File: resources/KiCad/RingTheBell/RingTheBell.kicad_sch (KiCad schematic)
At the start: 12 parts

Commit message: first cut at schematic
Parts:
- added SW1, SW2, SW3, SW4: SW_SPST, symbol Switch:SW_SPST
- renumbered U1 to A4
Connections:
- net at A3.~ (IO1_09), A4. (3V3), R2.2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: now also SW1.1 (A), SW2.1 (A)
- net at A2.~ (IO1_09): now also R6.2
- net at A1.~ (D13): now also R6.1; no longer A2.~ (IO1_09)
- net at A4. (3V3): now also A3.~ (IO1_09)
- net at A3.~ (IO1_09): no longer A4. (3V3)
- new net: A1.~ (D13), A2.~ (IO1_09), SW3.1 (A), SW4.1 (A)
- new net: A1.~ (D13), SW4.2 (B)
- new net: A1.~ (D13), A2.~ (IO1_09) (x3)
- new net: A1.~ (D13), SW3.2 (B)
- new net: A4. (3V3), SW2.2 (B)
- new net: A4. (3V3), SW1.2 (B)
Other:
- note added: "Purple-Mallet"
- note added: "White-Bell"
- note added: "Yellow"
- moved on the sheet: A3A, A4, LS1, R1, R2, R3, R4, R5

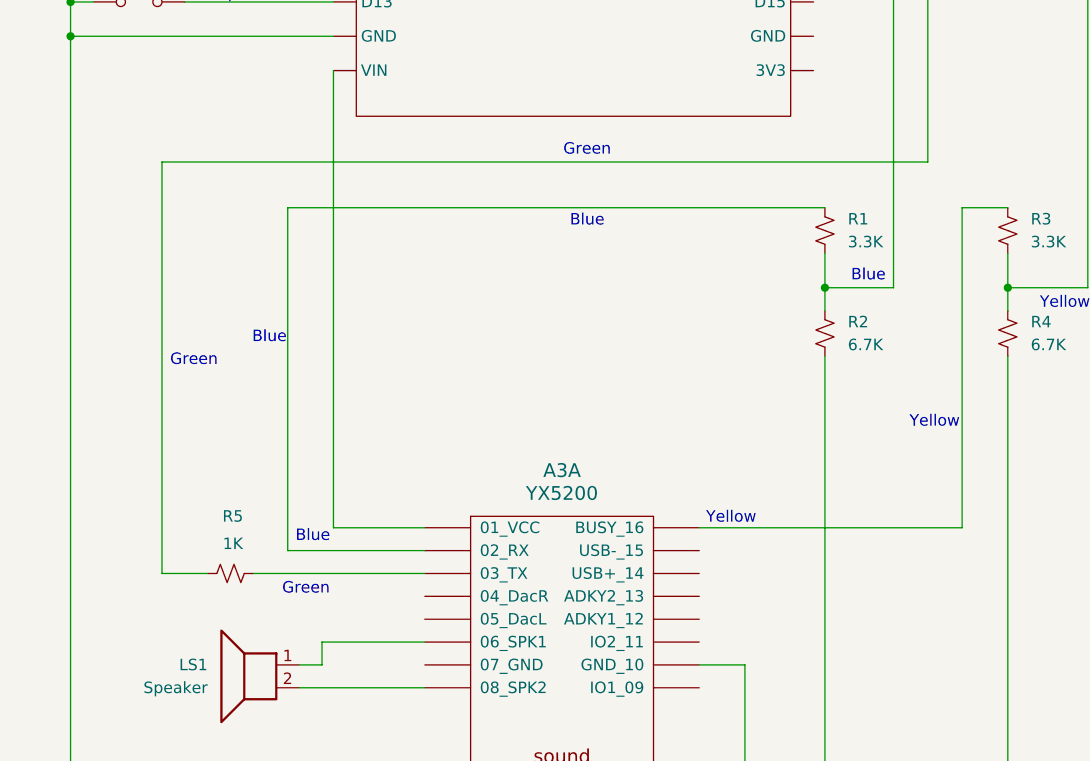
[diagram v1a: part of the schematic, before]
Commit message: fix error in ESP32 TX/RX
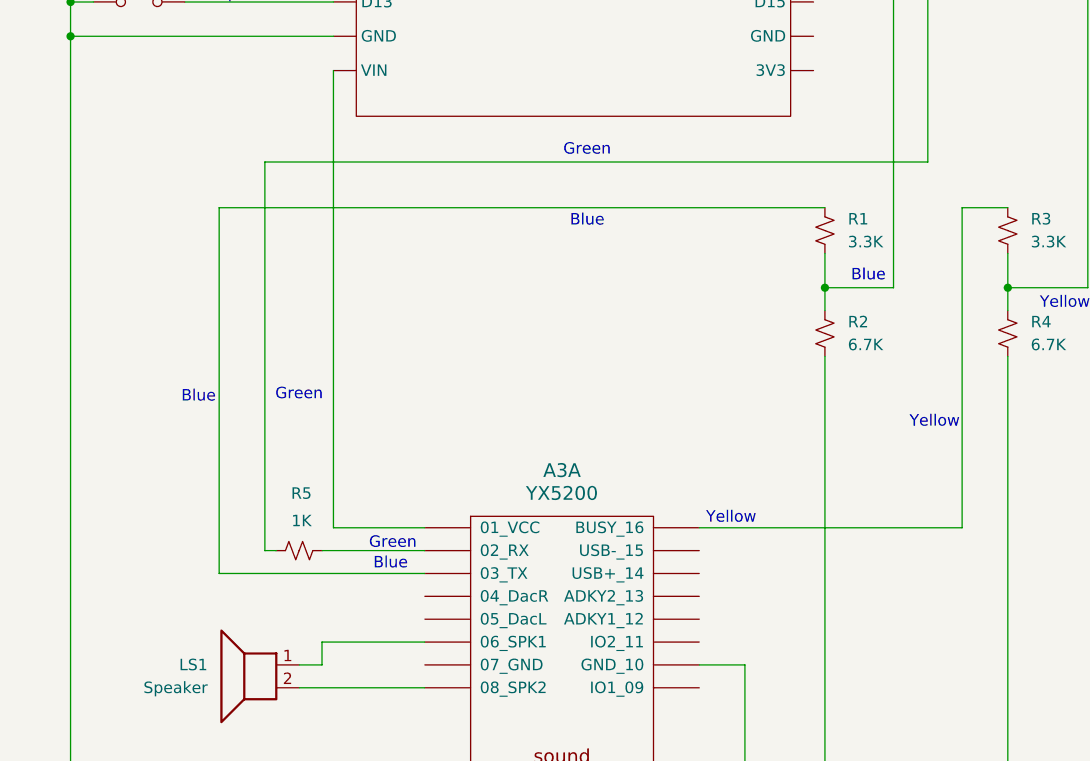
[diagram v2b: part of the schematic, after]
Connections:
- net at A2.~ (IO1_09): now also R6.2
- net at A1.~ (D13): now also R6.1; no longer A2.~ (IO1_09)
- net at A4. (3V3): now also A3.~ (IO1_09)
- net at A3.~ (IO1_09): no longer A4. (3V3)
- new net: A1.~ (D13), A2.~ (IO1_09) (x3)
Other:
- moved on the sheet: R5
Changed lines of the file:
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@@
 	(title_block
 		(title "RingTheBell")
-		(date "2025-06-13")
+		(date "2025-06-14")
 	)
 	(text "Yellow"
@@
 	(text "Green"
 		(exclude_from_sim no)
-		(at 149.606 110.998 0)
+		(at 161.29 114.808 0)
 		(effects
 			(font
@@
 	(text "Green"
 		(exclude_from_sim no)
-		(at 162.052 136.398 0)
+		(at 171.704 131.318 0)
 		(effects
 			(font
@@
 	(text "Blue"
 		(exclude_from_sim no)
-		(at 157.988 108.458 0)
+		(at 150.114 115.062 0)
 		(effects
 			(font
@@
 	(text "Blue"
 		(exclude_from_sim no)
-		(at 162.814 130.556 0)
+		(at 171.45 133.604 0)
 		(effects
 			(font
@@
 	(wire
 		(pts
-			(xy 146.05 88.9) (xy 231.14 88.9)
-		)
-		(stroke
-			(width 0)
-			(type default)
-		)
-	)
-	(wire
-		(pts
 			(xy 49.53 146.05) (xy 49.53 148.59)
 		)
@@
 	(wire
 		(pts
-			(xy 146.05 88.9) (xy 146.05 134.62)
-		)
-		(stroke
-			(width 0)
-			(type default)
-		)
-	)
-	(wire
-		(pts
 			(xy 163.83 142.24) (xy 175.26 142.24)
 		)
@@
 	(wire
 		(pts
-			(xy 175.26 132.08) (xy 160.02 132.08)
-		)
-		(stroke
-			(width 0)
-			(type default)
-		)
-	)
-	(wire
-		(pts
 			(xy 240.03 99.06) (xy 240.03 102.87)
 		)
@@
 	(wire
 		(pts
-			(xy 160.02 93.98) (xy 160.02 132.08)
+			(xy 248.92 102.87) (xy 240.03 102.87)
 		)
 		(stroke
@@
 	(wire
 		(pts
-			(xy 248.92 102.87) (xy 240.03 102.87)
+			(xy 135.89 163.83) (xy 210.82 163.83)
 		)
 		(stroke
@@
 	(wire
 		(pts
-			(xy 135.89 163.83) (xy 210.82 163.83)
+			(xy 161.29 147.32) (xy 175.26 147.32)
 		)
 		(stroke
@@
 	(wire
 		(pts
-			(xy 161.29 147.32) (xy 175.26 147.32)
+			(xy 93.98 133.35) (xy 100.33 133.35)
 		)
 		(stroke
@@
 	(wire
 		(pts
-			(xy 93.98 133.35) (xy 100.33 133.35)
+			(xy 63.5 60.96) (xy 48.26 60.96)
 		)
 		(stroke
@@
 	(wire
 		(pts
-			(xy 63.5 60.96) (xy 48.26 60.96)
+			(xy 135.89 74.93) (xy 135.89 163.83)
 		)
 		(stroke
@@
 	(wire
 		(pts
-			(xy 135.89 74.93) (xy 135.89 163.83)
+			(xy 157.48 88.9) (xy 231.14 88.9)
 		)
 		(stroke
@@
 	(wire
 		(pts
-			(xy 146.05 134.62) (xy 151.13 134.62)
+			(xy 175.26 134.62) (xy 152.4 134.62)
 		)
 		(stroke
@@
 	(wire
 		(pts
+			(xy 157.48 132.08) (xy 157.48 88.9)
+		)
+		(stroke
+			(width 0)
+			(type default)
+		)
+	)
+	(wire
+		(pts
 			(xy 219.71 163.83) (xy 240.03 163.83)
 		)
@@
 	(wire
 		(pts
-			(xy 156.21 134.62) (xy 175.26 134.62)
+			(xy 240.03 102.87) (xy 240.03 105.41)
 		)
 		(stroke
@@
 	(wire
 		(pts
-			(xy 240.03 102.87) (xy 240.03 105.41)
+			(xy 240.03 163.83) (xy 240.03 110.49)
 		)
 		(stroke
@@
 	(wire
 		(pts
-			(xy 240.03 163.83) (xy 240.03 110.49)
+			(xy 163.83 132.08) (xy 175.26 132.08)
 		)
 		(stroke
@@
 	(wire
 		(pts
+			(xy 158.75 132.08) (xy 157.48 132.08)
+		)
+		(stroke
+			(width 0)
+			(type default)
+		)
+	)
+	(wire
+		(pts
 			(xy 227.33 59.69) (xy 227.33 102.87)
 		)
@@
 	(wire
 		(pts
+			(xy 152.4 134.62) (xy 152.4 93.98)
+		)
+		(stroke
+			(width 0)
+			(type default)
+		)
+	)
+	(wire
+		(pts
 			(xy 44.45 148.59) (xy 49.53 148.59)
 		)
@@
 	(wire
 		(pts
+			(xy 152.4 93.98) (xy 219.71 93.98)
+		)
+		(stroke
+			(width 0)
+			(type default)
+		)
+	)
+	(wire
+		(pts
 			(xy 46.99 50.8) (xy 63.5 50.8)
 		)
@@
 	(wire
 		(pts
-			(xy 219.71 93.98) (xy 160.02 93.98)
-		)
-		(stroke
-			(width 0)
-			(type default)
-		)
-	)
-	(wire
-		(pts
 			(xy 104.14 33.02) (xy 104.14 148.59)
 		)
@@
 	(symbol
 		(lib_id "Device:R_Small_US")
-		(at 153.67 134.62 90)
+		(at 161.29 132.08 90)
 		(unit 1)
 		(exclude_from_sim no)
@@
 		(dnp no)
 		(property "Reference" "R5"
-			(at 153.924 128.27 90)
+			(at 161.544 125.73 90)
 			(effects
 				(font
@@
 		)
 		(property "Value" "1K"
-			(at 153.924 131.318 90)
+			(at 161.544 128.778 90)
 			(effects
 				(font
@@
 		)
 		(property "Footprint" ""
-			(at 153.67 134.62 0)
+			(at 161.29 132.08 0)
 			(effects
 				(font
@@
 		)
 		(property "Datasheet" "~"
-			(at 153.67 134.62 0)
+			(at 161.29 132.08 0)
 			(effects
 				(font
@@
 		)
 		(property "Description" "Resistor, small US symbol"
-			(at 153.67 134.62 0)
+			(at 161.29 132.08 0)
 			(effects
 				(font

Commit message: Various flavors of voltage levels
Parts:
- removed A3: YX5200, symbol mdoLibrary:YX5200
- removed A4: ~, symbol mdoLibrary:mdo_esp32_wroom
- removed LS1: Speaker, symbol Device:Speaker
- removed R1, R3: 3.3K, symbol Device:R_Small_US
- removed R2, R4: 6.7K, symbol Device:R_Small_US
- removed R5: 1K, symbol Device:R_Small_US
- removed SW1, SW2: SW_SPST, symbol Switch:SW_SPST
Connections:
- net at A2.~ (IO1_09): now also R6.2
- net at A1.~ (D13): now also R6.1; no longer A2.~ (IO1_09)
- new net: A1.~ (D13), A2.~ (IO1_09) (x3)
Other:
- added sheet 3.3V Power (3.3V.kicad_sch)
- added sheet 3.3V UART (3.3V_UART.kicad_sch)
- added sheet 74HCT125N (74HCT125N.kicad_sch)
- note added: "Arduino Nano/Uno and YX5200 5V Works Reliably"
- company: (none) -> https://github.com/Mark-MDO47/RingTheBell
- title: RingTheBell -> Ring the Bell Prototypes
- moved on the sheet: A1, A2A, LS2, R6, SW3, SW4

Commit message: tighten up the schematics
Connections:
- net at A2.~ (IO1_09): now also R6.2
- net at A1.~ (D13): now also R6.1; no longer A2.~ (IO1_09)
- new net: A1.~ (D13), A2.~ (IO1_09) (x3)
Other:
- moved on the sheet: A2A, LS2, R6
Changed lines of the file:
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@@
 	(title_block
 		(title "Ring the Bell Prototypes")
-		(date "2025-06-19")
+		(date "2025-06-20")
+		(rev "Rev 0.9")
 		(company "https://github.com/Mark-MDO47/RingTheBell")
 	)
 	(text "Yellow"
 		(exclude_from_sim no)
-		(at 71.374 117.348 0)
+		(at 71.374 100.838 0)
 		(effects
 			(font
@@
 	(text "Green"
 		(exclude_from_sim no)
-		(at 56.642 159.512 0)
+		(at 56.642 121.412 0)
 		(effects
 			(font
@@
 	(text "Blue"
 		(exclude_from_sim no)
-		(at 42.164 131.572 0)
+		(at 42.164 106.426 0)
 		(effects
 			(font
@@
 	(text "Green"
 		(exclude_from_sim no)
-		(at 51.816 131.572 0)
+		(at 51.816 106.426 0)
 		(effects
 			(font
@@
 	(text "Blue"
 		(exclude_from_sim no)
-		(at 56.388 161.798 0)
+		(at 56.388 123.698 0)
 		(effects
 			(font
@@
 	(text "Yellow"
 		(exclude_from_sim no)
-		(at 92.71 155.702 0)
+		(at 92.71 117.602 0)
 		(effects
 			(font
@@
 	(wire
 		(pts
-			(xy 55.88 139.7) (xy 55.88 157.48)
-		)
-		(stroke
-			(width 0)
-			(type default)
-		)
-	)
-	(wire
-		(pts
-			(xy 45.72 170.18) (xy 45.72 172.72)
+			(xy 45.72 132.08) (xy 45.72 134.62)
 		)
 		(stroke
@@
 	(wire
 		(pts
-			(xy 96.52 157.48) (xy 96.52 118.11)
-		)
-		(stroke
-			(width 0)
-			(type default)
-		)
-	)
-	(wire
-		(pts
-			(xy 59.69 170.18) (xy 45.72 170.18)
-		)
-		(stroke
-			(width 0)
-			(type default)
-		)
-	)
-	(wire
-		(pts
-			(xy 44.45 162.56) (xy 59.69 162.56)
-		)
-		(stroke
-			(width 0)
-			(type default)
-		)
-	)
-	(wire
-		(pts
-			(xy 44.45 85.09) (xy 44.45 162.56)
-		)
-		(stroke
-			(width 0)
-			(type default)
-		)
-	)
-	(wire
-		(pts
-			(xy 40.64 175.26) (xy 59.69 175.26)
+			(xy 59.69 132.08) (xy 45.72 132.08)
+		)
+		(stroke
+			(width 0)
+			(type default)
+		)
+	)
+	(wire
+		(pts
+			(xy 44.45 124.46) (xy 59.69 124.46)
+		)
+		(stroke
+			(width 0)
+			(type default)
+		)
+	)
+	(wire
+		(pts
+			(xy 40.64 137.16) (xy 59.69 137.16)
 		)
 		(stroke
@@
 	(wire
 		(pts
-			(xy 100.33 172.72) (xy 90.17 172.72)
+			(xy 90.17 134.62) (xy 100.33 134.62)
 		)
 		(stroke
@@
 	(wire
 		(pts
-			(xy 104.14 62.23) (xy 104.14 139.7)
+			(xy 104.14 62.23) (xy 104.14 109.22)
 		)
 		(stroke
@@
 	(wire
 		(pts
-			(xy 90.17 157.48) (xy 96.52 157.48)
+			(xy 90.17 119.38) (xy 96.52 119.38)
 		)
 		(stroke
@@
 	(wire
 		(pts
-			(xy 48.26 87.63) (xy 48.26 160.02)
+			(xy 48.26 87.63) (xy 48.26 121.92)
 		)
 		(stroke
@@
 	(wire
 		(pts
-			(xy 96.52 118.11) (xy 52.07 118.11)
+			(xy 96.52 101.6) (xy 52.07 101.6)
 		)
 		(stroke
@@
 	(wire
 		(pts
-			(xy 40.64 172.72) (xy 45.72 172.72)
-		)
-		(stroke
-			(width 0)
-			(type default)
-		)
-	)
-	(wire
-		(pts
-			(xy 53.34 160.02) (xy 59.69 160.02)
+			(xy 52.07 101.6) (xy 52.07 90.17)
+		)
+		(stroke
+			(width 0)
+			(type default)
+		)
+	)
+	(wire
+		(pts
+			(xy 96.52 101.6) (xy 96.52 119.38)
+		)
+		(stroke
+			(width 0)
+			(type default)
+		)
+	)
+	(wire
+		(pts
+			(xy 40.64 134.62) (xy 45.72 134.62)
+		)
+		(stroke
+			(width 0)
+			(type default)
+		)
+	)
+	(wire
+		(pts
+			(xy 53.34 121.92) (xy 59.69 121.92)
 		)
 		(stroke
@@
 	(wire
 		(pts
-			(xy 104.14 139.7) (xy 55.88 139.7)
-		)
-		(stroke
-			(width 0)
-			(type default)
-		)
-	)
-	(wire
-		(pts
-			(xy 55.88 157.48) (xy 59.69 157.48)
+			(xy 104.14 109.22) (xy 55.88 109.22)
+		)
+		(stroke
+			(width 0)
+			(type default)
+		)
+	)
+	(wire
+		(pts
+			(xy 55.88 109.22) (xy 55.88 119.38)
+		)
+		(stroke
+			(width 0)
+			(type default)
+		)
+	)
+	(wire
+		(pts
+			(xy 55.88 119.38) (xy 59.69 119.38)
 		)
 		(stroke
@@
 	(wire
 		(pts
-			(xy 52.07 118.11) (xy 52.07 90.17)
-		)
-		(stroke
-			(width 0)
-			(type default)
-		)
-	)
-	(wire
-		(pts
 			(xy 29.21 74.93) (xy 33.02 74.93)
 		)
@@
 	(wire
 		(pts
-			(xy 100.33 57.15) (xy 100.33 172.72)
+			(xy 100.33 57.15) (xy 100.33 134.62)
+		)
+		(stroke
+			(width 0)
+			(type default)
+		)
+	)
+	(wire
+		(pts
+			(xy 44.45 85.09) (xy 44.45 124.46)
 		)
 		(stroke
@@
 	(symbol
 		(lib_id "Device:Speaker")
-		(at 35.56 172.72 0)
+		(at 35.56 134.62 0)
 		(mirror y)
 		(unit 1)
@@
 		(dnp no)
 		(property "Reference" "LS2"
-			(at 30.48 172.7199 0)
+			(at 30.48 134.6199 0)
 			(effects
 				(font
@@
 		)
 		(property "Value" "Speaker"
-			(at 30.48 175.2599 0)
+			(at 30.48 137.1599 0)
 			(effects
 				(font
@@
 		)
 		(property "Footprint" ""
-			(at 35.56 177.8 0)
+			(at 35.56 139.7 0)
 			(effects
 				(font
@@
 		)
 		(property "Datasheet" "~"
-			(at 35.814 173.99 0)
+			(at 35.814 135.89 0)
 			(effects
 				(font
@@
 		)
 		(property "Description" "Speaker"
-			(at 35.56 172.72 0)
+			(at 35.56 134.62 0)
 			(effects
 				(font
@@
 	(symbol
 		(lib_id "mdoLibrary:YX5200")
-		(at 74.93 175.26 0)
+		(at 74.93 137.16 0)
 		(unit 1)
 		(exclude_from_sim no)
@@
 		(fields_autoplaced yes)
 		(property "Reference" "A2"
-			(at 74.93 151.13 0)
+			(at 74.93 113.03 0)
 			(effects
 				(font
@@
 		)
 		(property "Value" "YX5200"
-			(at 74.93 153.67 0)
+			(at 74.93 115.57 0)
 			(effects
 				(font
@@
 		)
 		(property "Footprint" ""
-			(at 74.93 175.26 0)
+			(at 74.93 137.16 0)
 			(effects
 				(font
@@
 		)
 		(property "Datasheet" ""
-			(at 74.93 175.26 0)
+			(at 74.93 137.16 0)
 			(effects
 				(font
@@
 		)
 		(property "Description" ""
-			(at 74.93 175.26 0)
+			(at 74.93 137.16 0)
 			(effects
 				(font
@@
 	(symbol
 		(lib_id "Device:R_Small_US")
-		(at 50.8 160.02 90)
+		(at 50.8 121.92 90)
 		(unit 1)
 		(exclude_from_sim no)
@@
 		(dnp no)
 		(property "Reference" "R6"
-			(at 51.054 153.67 90)
+			(at 51.054 115.57 90)
 			(effects
 				(font
@@
 		)
 		(property "Value" "1K"
-			(at 51.054 156.718 90)
+			(at 51.054 118.618 90)
 			(effects
 				(font
@@
 		)
 		(property "Footprint" ""
-			(at 50.8 160.02 0)
+			(at 50.8 121.92 0)
 			(effects
 				(font
@@
 		)
 		(property "Datasheet" "~"
-			(at 50.8 160.02 0)
+			(at 50.8 121.92 0)
 			(effects
 				(font
@@
 		)
 		(property "Description" "Resistor, small US symbol"
-			(at 50.8 160.02 0)
-			(effects
-				(font
+			(at 50.8 121.92 0)
+			(effects
+				(font
